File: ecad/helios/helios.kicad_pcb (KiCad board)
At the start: 2 copper layers, 84.3 x 41 mm, 72 parts, among them J1 JST SH, J2 JST SH, J3 Jack-DC OD 5.5 IN 2.1, J4 JST XH, J5 JST XH, J6 JST XH, J7 JST XH, J8 Conn_01x08, U2 RP2040, U4 THVD8010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

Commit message: [WIP] Layouting Helios
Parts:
- added C31: 100n, Capacitor_SMD:C_0402_1005Metric, F.Cu at (166.8, 101.2)
- added C32: 1n, Capacitor_SMD:C_0402_1005Metric, F.Cu at (135.8, 94.7)
- added C34: 100n, Capacitor_SMD:C_0402_1005Metric, F.Cu at (139.2, 91.6)
- added D5: CDSOT23-T24CAN, Package_TO_SOT_SMD:SOT-23, F.Cu at (148.5, 104.0)
- added D6: BAT54J, Diode_SMD:D_SOD-323F, F.Cu at (134.3, 93.8)
- added J10: JST PH, fort:JST_PH_B4B-PH-SM4-TB_1x04-1MP_P2.00mm_Vertical, F.Cu at (134.2, 106.0)
- added J11: Phoenix MCV_1,5, Connector_Phoenix_MC:PhoenixContact_MCV_1,5_2-G-3.5_1x02_P3.50mm_Vertical, F.Cu at (154.4, 86.9)
- added J12: Phoenix MCV_1,5, Connector_Phoenix_MC:PhoenixContact_MCV_1,5_2-G-3.5_1x02_P3.50mm_Vertical, F.Cu at (145.0, 86.9)
- added J13: Phoenix MCV_1,5, Connector_Phoenix_MC:PhoenixContact_MCV_1,5_2-G-3.5_1x02_P3.50mm_Vertical, F.Cu at (135.0, 86.9)
- added J15: Phoenix MCV_1,5, Connector_Phoenix_MC:PhoenixContact_MCV_1,5_2-G-3.5_1x02_P3.50mm_Vertical, F.Cu at (187.8, 86.9)
- added J16: Phoenix MCV_1,5, Connector_Phoenix_MC:PhoenixContact_MCV_1,5_2-G-3.5_1x02_P3.50mm_Vertical, F.Cu at (197.2, 86.9)
- added J17: Phoenix MCV_1,5, Connector_Phoenix_MC:PhoenixContact_MCV_1,5_2-G-3.5_1x02_P3.50mm_Vertical, F.Cu at (177.8, 86.9)
- added J9: JST PH, fort:JST_PH_B4B-PH-SM4-TB_1x04-1MP_P2.00mm_Vertical, F.Cu at (142.8, 106.0)
- added JP1: Term, Connector_PinHeader_2.54mm:PinHeader_1x02_P2.54mm_Vertical, F.Cu at (127.6, 103.9)
- added JP2: .100 Header, Connector_PinHeader_2.54mm:PinHeader_1x03_P2.54mm_Vertical, F.Cu at (134.3, 97.5)
- added Q1: RE1C002UN, Package_TO_SOT_SMD:SOT-416, F.Cu at (187.7, 101.3)
- added Q2: RE1C002UN, Package_TO_SOT_SMD:SOT-416, F.Cu at (200.7, 101.3)
- added Q3: DMG2305UX, Package_TO_SOT_SMD:SOT-23, F.Cu at (177.7, 92.4)
- added R13: 120, Resistor_SMD:R_0402_1005Metric, F.Cu at (128.5, 106.2)
- added R14: 1k, Resistor_SMD:R_0402_1005Metric, F.Cu at (150.2, 103.6)
- added R15: 180, Resistor_SMD:R_0402_1005Metric, F.Cu at (162.4, 93.9)
- added R16: 1k, Resistor_SMD:R_0402_1005Metric, F.Cu at (150.2, 104.6)
- added R17: 180, Resistor_SMD:R_0402_1005Metric, F.Cu at (150.6, 93.9)
- added R18: 15k, Resistor_SMD:R_0402_1005Metric, F.Cu at (137.3, 91.6)
- added R19: 15k, Resistor_SMD:R_0402_1005Metric, F.Cu at (135.8, 92.8)
- added R22: 220, Resistor_SMD:R_0402_1005Metric, F.Cu at (187.9, 99.6)
- added R23: 220, Resistor_SMD:R_0402_1005Metric, F.Cu at (200.5, 99.6)
- added R24: 15k, Resistor_SMD:R_0402_1005Metric, F.Cu at (177.7, 94.9)
- added REF**: MountingHole_2.7mm_M2.5, MountingHole:MountingHole_2.7mm_M2.5, F.Cu at (129.0, 90.0)
- added U1: W25Q16JVUXIQ, fort:Winbond_USON-8-1EP_UX_2x3mm_P0.5mm_EP0.2x1.5mm, F.Cu at (161.6, 110.9)
- added U10: LTV-827S, Package_DIP:SMDIP-8_W9.53mm, F.Cu at (156.5, 99.0)
- added U12: LTV-827S, Package_DIP:SMDIP-8_W9.53mm, F.Cu at (194.2, 96.5)
- added U3: LMR36501P3RPE, fort:Texas_VQFN-HR-9_2.1x2.1mm_P0.5mm, F.Cu at (151.0, 107.7)
- added U8: TCAN3414, Package_TO_SOT_SMD:SOT-23-8, F.Cu at (164.2, 101.2)
- added U9: 74LVC1G17, Package_TO_SOT_SMD:SOT-23-5, F.Cu at (138.4, 93.8)
- J1: moved to B.Cu
- J8: value Conn_01x08 -> .100 Header
- L1: value 47u -> 47u
- L2, L3, L4, L5, L6, L7, L8, L9: value 350u -> 330u
- moved C1 143.4 mm to (178.1, 111.1), turned to 180 degrees
- moved C2 139.9 mm to (178.1, 105.9)
- moved Y1 135.2 mm to (178.1, 108.5), turned to 90 degrees
- moved R1 135.0 mm to (190.5, 106.3)
- moved C5 134.8 mm to (175.3, 106.0)
- moved U2 134.6 mm to (169.2, 108.0), turned to 90 degrees
- moved C11 134.1 mm to (175.3, 107.0)
- moved C12 131.9 mm to (170.2, 113.1), turned to -90 degrees
- moved C13 127.7 mm to (166.3, 113.1), turned to -90 degrees
- moved C6 126.6 mm to (159.6, 112.8), turned to 180 degrees
- moved C4 126.5 mm to (163.6, 108.3), turned to 180 degrees
- moved C3 126.5 mm to (163.6, 106.3), turned to 180 degrees
- moved C10 126.2 mm to (170.2, 102.9), turned to 90 degrees
- moved C8 124.6 mm to (163.6, 107.3), turned to 180 degrees
- moved C7 124.5 mm to (163.6, 105.3), turned to 180 degrees
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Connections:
- U2 pad 11: unconnected-(U2-GPIO8-Pad11) -> /~{OUT_HS1}
- U2 pad 12: unconnected-(U2-GPIO9-Pad12) -> /~{OUT_HS2}
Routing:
- net +3V3: track 84.7 -> 115.2 mm
- net +1V1: track 0.00 -> 18.9 mm, vias 0 -> 4
- net /QSPI_IO3: track 0.00 -> 9.60 mm
- net GND: track 16.1 -> 25.3 mm, vias 40 -> 52
- net /XIN: track 0.00 -> 8.50 mm
- net /QSPI_SCLK: track 0.00 -> 8.26 mm
- net /QSPI_IO0: track 0.00 -> 5.97 mm
- net /XOUT_NP: track 0.00 -> 3.25 mm
- net /QSPI_SS: track 0.00 -> 3.10 mm
- net /QSPI_IO1: track 0.00 -> 3.06 mm
- net /QSPI_IO2: track 0.00 -> 3.02 mm
- net /SWDIO: track 0.00 -> 2.97 mm
- net /XOUT: track 0.00 -> 2.33 mm
- net /SWCLK: track 0.00 -> 2.07 mm
- net /RUN: track 0.00 -> 1.57 mm
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- added copper zone on F.Cu, net +1V1
- added copper zone on F.Cu, net +3V3
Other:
- board outline removed

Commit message: Layouts Helios MkII
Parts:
- removed J16, J17: Phoenix MCV_1,5, Connector_Phoenix_MC:PhoenixContact_MCV_1,5_2-G-3.5_1x02_P3.50mm_Vertical
- removed Q1, Q2: RE1C002UN, Package_TO_SOT_SMD:SOT-416
- removed Q3: DMG2305UX, Package_TO_SOT_SMD:SOT-23
- removed R22, R23: 220, Resistor_SMD:R_0402_1005Metric
- removed R24: 15k, Resistor_SMD:R_0402_1005Metric
- added C33: 100n, Capacitor_SMD:C_0402_1005Metric, F.Cu at (136.4, 90.0)
- added C35: 100n, Capacitor_SMD:C_0402_1005Metric, F.Cu at (145.9, 90.1)
- added D7: GREEN, LED_SMD:LED_0603_1608Metric, F.Cu at (186.1, 85.8)
- added D8: YELLOW, LED_SMD:LED_0603_1608Metric, F.Cu at (183.1, 85.8)
- added J14: Phoenix MCV_1,5, Connector_Phoenix_MC:PhoenixContact_MCV_1,5_2-G-3.5_1x02_P3.50mm_Vertical, F.Cu at (135.2, 85.8)
- added U11: 74LVC1G17, Package_TO_SOT_SMD:SOT-23-5, F.Cu at (136.9, 92.6)
- J1: moved to F.Cu
- L1: value 47u -> 22u; footprint Inductor_SMD:L_Taiyo-Yuden_NR-40xx -> fort:L_Wuerth_WE-LQS_4025
- R3: value 7.5k -> 60
- R4: value 10k -> 240
- U12: value LTV-827S -> 74LVC1G17; footprint Package_DIP:SMDIP-8_W9.53mm -> Package_TO_SOT_SMD:SOT-23-5
- U3: value LMR36501P3RPE -> LMR36502P3RPE
- moved U12 47.9 mm to (146.4, 92.7)
- moved R3 43.2 mm to (186.1, 88.2), turned to -90 degrees
- moved J15 43.2 mm to (144.6, 85.8)
- moved R4 40.1 mm to (183.1, 88.2), turned to -90 degrees
- moved R1 20.8 mm to (169.8, 104.3), turned to 90 degrees
- moved J3 20.2 mm to (199.2, 94.9), turned to -90 degrees
- moved J11 19.6 mm to (174.0, 85.8)
- moved J12 19.6 mm to (164.6, 85.8)
- moved J13 19.6 mm to (154.6, 85.8)
- moved C32 18.1 mm to (153.8, 93.0)
- moved C34 18.1 mm to (157.2, 89.9)
- moved JP2 18.1 mm to (152.3, 95.8)
- moved R18 18.1 mm to (155.3, 89.9)
- moved R19 18.1 mm to (153.8, 91.1)
- moved U9 18.1 mm to (156.4, 92.1)
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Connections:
- J15 pad 2: Net-(J15-Pin_2) -> GND
- JP1 pad 2: /CAN- -> /CAN+
- R13 pad 2: /CAN+ -> /CAN-
- R3 pad 1: +12V -> Net-(D7-A)
- R3 pad 2: /RG_EN -> /LED_G
- R4 pad 1: /RG_EN -> Net-(D8-A)
- R4 pad 2: GND -> /LED_Y
- U12 pad 1: Net-(R22-Pad1) -> unconnected-(U12-NC-Pad1)
- U12 pad 2: Net-(Q1-D) -> /OUT_2
- U12 pad 3: Net-(R23-Pad1) -> GND
- U12 pad 4: Net-(Q2-D) -> Net-(J15-Pin_1)
- U12 pad 5: Net-(J16-Pin_2) -> +3V3
- U2 pad 11: /~{OUT_HS1} -> /TX
- U2 pad 12: /~{OUT_HS2} -> unconnected-(U2-GPIO9-Pad12)
- U2 pad 14: unconnected-(U2-GPIO11-Pad14) -> /LED_G
- U2 pad 15: /CAN_TX -> /LED_Y
- U2 pad 16: /CAN_RX -> unconnected-(U2-GPIO13-Pad16)
- U2 pad 17: /CAN_SHUTDOWN -> unconnected-(U2-GPIO14-Pad17)
- U2 pad 18: /CAN_STDBY -> unconnected-(U2-GPIO15-Pad18)
- U2 pad 30: unconnected-(U2-GPIO19-Pad30) -> /IN_ISO1
- U2 pad 31: unconnected-(U2-GPIO20-Pad31) -> /IN_ISO2
- U2 pad 34: /PWM_FAN -> unconnected-(U2-GPIO22-Pad34)
- U2 pad 35: /PWM_HEAT -> /IN_OC1
- U2 pad 36: unconnected-(U2-GPIO24-Pad36) -> /OUT_2
- U2 pad 37: unconnected-(U2-GPIO25-Pad37) -> /OUT_1
- U2 pad 38: unconnected-(U2-GPIO26_ADC0-Pad38) -> /CAN_SHUTDOWN
- U2 pad 39: unconnected-(U2-GPIO27_ADC1-Pad39) -> /CAN_STDBY
- U2 pad 4: unconnected-(U2-GPIO2-Pad4) -> /DE
- U2 pad 40: unconnected-(U2-GPIO28_ADC2-Pad40) -> /CAN_TX
- U2 pad 41: unconnected-(U2-GPIO29_ADC3-Pad41) -> /CAN_RX
- U2 pad 7: /DE -> unconnected-(U2-GPIO5-Pad7)
- U2 pad 8: /TX -> unconnected-(U2-GPIO6-Pad8)
- U3 pad 3: /RG_EN -> +12V
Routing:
- net +3V3: track 115.2 -> 279.8 mm, vias 0 -> 1
- net /CAN+: track 0.00 -> 101.0 mm
- net /CAN-: track 0.00 -> 94.9 mm
- net GND: track 25.3 -> 68.1 mm, vias 52 -> 103
- net /LED_G: track 0.00 -> 39.4 mm
- net /OUT_1: track 0.00 -> 36.6 mm
- net /LED_Y: track 0.00 -> 35.4 mm
- net /TX: track 79.1 -> 107.4 mm
- net /OUT_2: track 0.00 -> 27.6 mm
- net /RUN: track 1.57 -> 25.5 mm, vias 0 -> 2
- net +48V: track 115.3 -> 136.4 mm
- net /IN_ISO1: track 0.00 -> 20.9 mm
- net /IN_OC1: track 0.00 -> 18.6 mm
- net +12V: track 0.00 -> 16.7 mm
- net Net-(J11-Pin_2): track 0.00 -> 14.4 mm
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- added copper zone on F.Cu, net +12V
- added copper zone on F.Cu, net /RG_SW
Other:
- board outline added: 84 x 60 mm
- board text added: "DBG"
- board text added: "ERR"
- board text added: "FLTR1"
- board text added: "FORT Helios MkII Illumination Controller Rev A"
- board text added: "ISO1"
- board text added: "ISO2"
- board text added: "Off"
- board text added: "On"
- board text added: "STS"
- board text added: "SWD"
- board text added: "TTL1"
- board text added: "TTL2"
- board text added: "© 2024 Université de Genève"

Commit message: Adds TVS to Helios
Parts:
- added D10: SMAJ51CA, Diode_SMD:D_SMA, B.Cu at (145.2, 135.4)
- added D11: SMAJ51CA, Diode_SMD:D_SMA, B.Cu at (181.2, 135.4)
- added D12: SMAJ51CA, Diode_SMD:D_SMA, B.Cu at (199.2, 135.4)
- added D13: SMAJ48CA, Diode_SMD:D_SMA, F.Cu at (205.8, 91.7)
- added D9: SMAJ51CA, Diode_SMD:D_SMA, B.Cu at (163.2, 135.4)
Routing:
- net +48V: track 136.4 -> 143.5 mm
- net GND: track 68.1 -> 75.1 mm
- net /Transmitter3/RX-: track 33.6 -> 37.4 mm
- net /Transmitter2/RX-: track 33.6 -> 37.4 mm
- net /Transmitter1/RX-: track 33.6 -> 37.4 mm
- net /Transmitter0/RX-: track 33.1 -> 36.9 mm
- net /Transmitter3/RX+: track 9.69 -> 13.4 mm
- net /Transmitter2/RX+: track 9.69 -> 13.4 mm
- net /Transmitter1/RX+: track 9.69 -> 13.4 mm
- net /Transmitter0/RX+: track 9.69 -> 13.4 mm

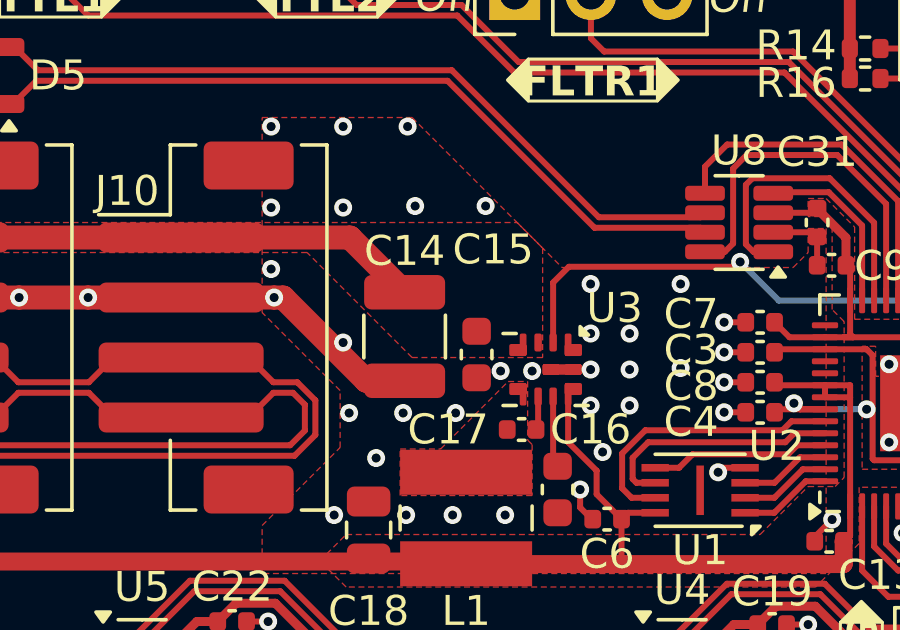
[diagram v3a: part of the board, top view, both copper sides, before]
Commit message: Updates MPN for new PCBs
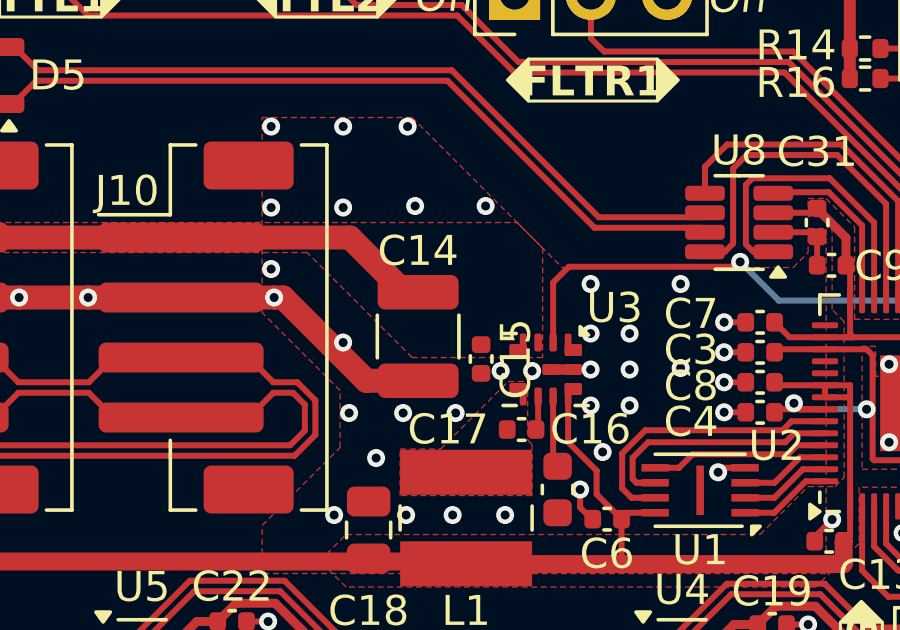
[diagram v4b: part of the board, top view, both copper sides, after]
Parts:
- C15: footprint Capacitor_SMD:C_0603_1608Metric -> Capacitor_SMD:C_0402_1005Metric
- J8: value .100 Header -> .100 Header stackable
- R1: value 10k -> 15k
- R3: value 60 -> 62
- moved C14 0.45 mm to (149.1, 107.2)
- moved C15 0.21 mm to (151.2, 108.0)
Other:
- board text added: "WayWayWay"

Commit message: upload to pcbway
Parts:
- added REF**: OSHW-Logo_7.5x8mm_SilkScreen, Symbol:OSHW-Logo_7.5x8mm_SilkScreen, B.Cu at (202.2, 111.5)
- added TP1: 5019, TestPoint:TestPoint_Keystone_5019_Minature, F.Cu at (181.6, 101.7)
- added TP10: 5019, TestPoint:TestPoint_Keystone_5019_Minature, B.Cu at (183.6, 138.7)
- added TP11: 5019, TestPoint:TestPoint_Keystone_5019_Minature, B.Cu at (201.6, 138.7)
- added TP12: 5019, TestPoint:TestPoint_Keystone_5019_Minature, F.Cu at (204.3, 113.8)
- added TP13: 5019, TestPoint:TestPoint_Keystone_5019_Minature, F.Cu at (198.5, 113.9)
- added TP2: 5019, TestPoint:TestPoint_Keystone_5019_Minature, F.Cu at (181.6, 97.0)
- added TP3: 5019, TestPoint:TestPoint_Keystone_5019_Minature, F.Cu at (201.4, 108.5)
- added TP4: 5019, TestPoint:TestPoint_Keystone_5019_Minature, B.Cu at (160.9, 138.7)
- added TP5: 5019, TestPoint:TestPoint_Keystone_5019_Minature, B.Cu at (142.9, 138.7)
- added TP6: 5019, TestPoint:TestPoint_Keystone_5019_Minature, B.Cu at (178.9, 138.7)
- added TP7: 5019, TestPoint:TestPoint_Keystone_5019_Minature, B.Cu at (196.9, 138.7)
- added TP8: 5019, TestPoint:TestPoint_Keystone_5019_Minature, B.Cu at (165.6, 138.7)
- added TP9: 5019, TestPoint:TestPoint_Keystone_5019_Minature, B.Cu at (147.6, 138.7)
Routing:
- net /IN_ISO2: track 11.5 -> 30.7 mm
- net +3V3: track 279.8 -> 291.2 mm
- net /IN_ISO1: track 20.9 -> 29.1 mm
- net GND: track 75.1 -> 78.9 mm
- net /Transmitter3/RX+: track 13.4 -> 16.8 mm
- net /Transmitter2/RX+: track 13.4 -> 16.8 mm
- net /Transmitter1/RX+: track 13.4 -> 16.8 mm
- net /Transmitter0/RX+: track 13.4 -> 16.8 mm
- net /Transmitter3/RX-: track 37.4 -> 40.8 mm
- net /Transmitter2/RX-: track 37.4 -> 40.8 mm
- net /Transmitter1/RX-: track 37.4 -> 40.8 mm
- net /Transmitter0/RX-: track 36.9 -> 40.3 mm
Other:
- board text added: "3V3"
- board text added: "48V"
- board text added: "GND"
- board text added: "RX+"
- board text added: "RX-"

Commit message: WIP
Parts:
- U3: value LMR36502P3RPE -> LMR36506R3RPER
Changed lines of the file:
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@@
 			)
 		)
+		(property "MPN" "5019"
+			(at 0 0 90)
+			(unlocked yes)
+			(layer "F.Fab")
+			(hide yes)
+			(effects
+				(font
+					(size 1 1)
+					(thickness 0.15)
+				)
+			)
+		)
 		(property ki_fp_filters "Pin* Test*")
 		(sheetname "Root")
@@
 			)
 		)
-		(property "Value" "LMR36502P3RPE"
+		(property "Value" "LMR36506R3RPER"
 			(at -0.05 2.45 -90)
 			(unlocked yes)
@@
 			)
 		)
-		(property "Datasheet" "https://www.ti.com/lit/ds/symlink/lmr36502.pdf"
+		(property "Datasheet" "https://www.ti.com/lit/ds/symlink/lmr36506.pdf"
 			(at 0 0 -90)
 			(unlocked yes)
@@
 			)
 		)
-		(property "Description" "Synchronous Buck Regulator, Vin=3-65V, Iout=150mA, F=0.2-2.2MHz, Adjustable output voltage, PFM at light load, VQFN-HR RPE"
+		(property "Description" "Synchronous Buck Regulator, Vin=3-65V, Iout=600mA, F=0.2-2.2MHz, Adjustable output voltage, PFM at light load, VQFN-HR RPE"
 			(at 0 0 -90)
 			(unlocked yes)
@@
 			)
 		)
-		(property "Manufacturer" ""
-			(at 0 0 -90)
-			(unlocked yes)
-			(layer "F.Fab")
-			(hide yes)
-			(effects
-				(font
-					(size 1 1)
-					(thickness 0.15)
-				)
-			)
-		)
-		(property "MPN" "LMR36502P3RPE"
+		(property "MPN" "LMR36506R3RPER"
 			(at 0 0 -90)
 			(unlocked yes)
@@
 			)
 		)
+		(property "MPN" "5019"
+			(at 0 0 90)
+			(unlocked yes)
+			(layer "F.Fab")
+			(hide yes)
+			(effects
+				(font
+					(size 1 1)
+					(thickness 0.15)
+				)
+			)
+		)
 		(property ki_fp_filters "Pin* Test*")
 		(sheetname "Root")
@@
 			)
 		)
+		(property "MPN" "5019"
+			(at 0 0 90)
+			(unlocked yes)
+			(layer "F.Fab")
+			(hide yes)
+			(effects
+				(font
+					(size 1 1)
+					(thickness 0.15)
+				)
+			)
+		)
 		(property ki_fp_filters "Pin* Test*")
 		(sheetname "Root")
@@
 			)
 		)
+		(property "MPN" "5019"
+			(at 0 0 90)
+			(unlocked yes)
+			(layer "F.Fab")
+			(hide yes)
+			(effects
+				(font
+					(size 1 1)
+					(thickness 0.15)
+				)
+			)
+		)
 		(property ki_fp_filters "Pin* Test*")
 		(sheetname "Root")
@@
 			)
 		)
+		(property "MPN" "5019"
+			(at 0 0 90)
+			(unlocked yes)
+			(layer "F.Fab")
+			(hide yes)
+			(effects
+				(font
+					(size 1 1)
+					(thickness 0.15)
+				)
+			)
+		)
 		(property ki_fp_filters "Pin* Test*")
 		(sheetname "Root")
@@
 			)
 		)
+		(property "MPN" "5019"
+			(at 0 0 180)
+			(unlocked yes)
+			(layer "B.Fab")
+			(hide yes)
+			(effects
+				(font
+					(size 1 1)
+					(thickness 0.15)
+				)
+				(justify mirror)
+			)
+		)
 		(property ki_fp_filters "Pin* Test*")
 		(sheetname "Transmitter0")
@@
 			)
 		)
+		(property "MPN" "5019"
+			(at 0 0 180)
+			(unlocked yes)
+			(layer "B.Fab")
+			(hide yes)
+			(effects
+				(font
+					(size 1 1)
+					(thickness 0.15)
+				)
+				(justify mirror)
+			)
+		)
 		(property ki_fp_filters "Pin* Test*")
 		(sheetname "Transmitter3")
@@
 			)
 		)
+		(property "MPN" "5019"
+			(at 0 0 180)
+			(unlocked yes)
+			(layer "B.Fab")
+			(hide yes)
+			(effects
+				(font
+					(size 1 1)
+					(thickness 0.15)
+				)
+				(justify mirror)
+			)
+		)
 		(property ki_fp_filters "Pin* Test*")
 		(sheetname "Transmitter2")
@@
 			)
 		)
+		(property "MPN" "5019"
+			(at 0 0 180)
+			(unlocked yes)
+			(layer "B.Fab")
+			(hide yes)
+			(effects
+				(font
+					(size 1 1)
+					(thickness 0.15)
+				)
+				(justify mirror)
+			)
+		)
 		(property ki_fp_filters "Pin* Test*")
 		(sheetname "Transmitter1")
@@
 			)
 		)
+		(property "MPN" "5019"
+			(at 0 0 180)
+			(unlocked yes)
+			(layer "B.Fab")
+			(hide yes)
+			(effects
+				(font
+					(size 1 1)
+					(thickness 0.15)
+				)
+				(justify mirror)
+			)
+		)
 		(property ki_fp_filters "Pin* Test*")
 		(sheetname "Transmitter3")
@@
 			)
 		)
+		(property "MPN" "5019"
+			(at 0 0 180)
+			(unlocked yes)
+			(layer "B.Fab")
+			(hide yes)
+			(effects
+				(font
+					(size 1 1)
+					(thickness 0.15)
+				)
+				(justify mirror)
+			)
+		)
 		(property ki_fp_filters "Pin* Test*")
 		(sheetname "Transmitter1")
@@
 			)
 		)
+		(property "MPN" "5019"
+			(at 0 0 180)
+			(unlocked yes)
+			(layer "B.Fab")
+			(hide yes)
+			(effects
+				(font
+					(size 1 1)
+					(thickness 0.15)
+				)
+				(justify mirror)
+			)
+		)
 		(property ki_fp_filters "Pin* Test*")
 		(sheetname "Transmitter0")
@@
 					(thickness 0.15)
 				)
+				(justify mirror)
+			)
+		)
+		(property "MPN" "5019"
+			(at 0 0 180)
+			(unlocked yes)
+			(layer "B.Fab")
+			(hide yes)
+			(effects
+				(font
+					(size 1 1)
+					(thickness 0.15)
+				)

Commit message: Backports changes forgotten on Friday
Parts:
- C18: value 10u -> 22u
- L1: value 22u -> 8.2u; footprint fort:L_Wuerth_WE-LQS_4025 -> fort:L_Wuerth_WE-SPC_4838
- moved J10 1.00 mm to (140.7, 106.9)
- moved J9 1.00 mm to (132.2, 106.9)
- moved C18 0.95 mm to (146.5, 113.7)
- moved L1 0.54 mm to (150.2, 113.5)
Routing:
- net +3V3: track 291.2 -> 320.6 mm, vias 1 -> 0
- net /CAN+: track 101.0 -> 102.3 mm
- net /CAN-: track 94.9 -> 96.3 mm
- net GND: track 78.9 -> 79.9 mm
- net +12V: track 16.7 -> 17.7 mm

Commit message: Updates PCBs
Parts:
- J1, J2: footprint Connector_JST:JST_SH_BM03B-SRSS-TB_1x03-1MP_P1.00mm_Vertical -> fort:JST_SH_BM03B-SRSS-TB_1x03-1MP_P1.00mm_Vertical
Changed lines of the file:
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@@
 		)
 	)
-	(footprint "Connector_JST:JST_SH_BM03B-SRSS-TB_1x03-1MP_P1.00mm_Vertical"
+	(footprint "fort:JST_SH_BM03B-SRSS-TB_1x03-1MP_P1.00mm_Vertical"
 		(layer "F.Cu")
 		(at 173.7 104.1 180)
@@
 		(tags "connector JST SH vertical")
 		(property "Reference" "J2"
-			(at -2.6 1.95 0)
+			(at 0 -3.3 180)
 			(layer "F.SilkS")
 			(effects
@@
 		)
 		(property "Value" "JST SH"
-			(at 0 3.3 0)
+			(at 0 3.3 180)
 			(layer "F.Fab")
 			(effects
@@
 			)
 		)
-		(property "Footprint" "Connector_JST:JST_SH_BM03B-SRSS-TB_1x03-1MP_P1.00mm_Vertical"
+		(property "Footprint" "fort:JST_SH_BM03B-SRSS-TB_1x03-1MP_P1.00mm_Vertical"
 			(at 0 0 180)
 			(unlocked yes)
@@
 		)
 		(fp_text user "${REFERENCE}"
-			(at 0 -0.25 0)
+			(at 0 -0.25 180)
 			(layer "F.Fab")
 			(effects
@@
 			(roundrect_rratio 0.208333)
 		)
-		(model "${KICAD8_3DMODEL_DIR}/Connector_JST.3dshapes/JST_SH_BM03B-SRSS-TB_1x03-1MP_P1.00mm_Vertical.wrl"
+		(model "${KIPRJMOD}/lib/fort.3dshapes/BM03B-SRSS-TB.STEP"
 			(offset
-				(xyz 0 0 0)
+				(xyz 0 1.15 0)
 			)
 			(scale
@@
 			)
 			(rotate
-				(xyz 0 0 0)
+				(xyz -90 0 0)
 			)
 		)
@@
 		)
 	)
-	(footprint "Connector_JST:JST_SH_BM03B-SRSS-TB_1x03-1MP_P1.00mm_Vertical"
+	(footprint "fort:JST_SH_BM03B-SRSS-TB_1x03-1MP_P1.00mm_Vertical"
 		(layer "F.Cu")
 		(at 167.6 117.35 180)
@@
 		(tags "connector JST SH vertical")
 		(property "Reference" "J1"
-			(at -2.55 1.85 180)
+			(at 0 -3.3 180)
 			(layer "F.SilkS")
 			(effects
@@
 			)
 		)
-		(property "Footprint" "Connector_JST:JST_SH_BM03B-SRSS-TB_1x03-1MP_P1.00mm_Vertical"
+		(property "Footprint" "fort:JST_SH_BM03B-SRSS-TB_1x03-1MP_P1.00mm_Vertical"
 			(at 0 0 180)
 			(unlocked yes)
@@
 		(sheetname "Root")
 		(sheetfile "helios.kicad_sch")
-		(attr smd dnp)
+		(attr smd)
 		(fp_line
 			(start 2.61 1.11)
@@
 			(roundrect_rratio 0.208333)
 		)
-		(model "${KICAD8_3DMODEL_DIR}/Connector_JST.3dshapes/JST_SH_BM03B-SRSS-TB_1x03-1MP_P1.00mm_Vertical.wrl"
+		(model "${KIPRJMOD}/lib/fort.3dshapes/BM03B-SRSS-TB.STEP"
 			(offset
-				(xyz 0 0 0)
+				(xyz 0 1.15 0)
 			)
 			(scale
@@
 			)
 			(rotate
-				(xyz 0 0 0)
+				(xyz -90 0 0)
 			)
 		)
